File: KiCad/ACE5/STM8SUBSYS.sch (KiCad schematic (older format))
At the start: 4 parts, among them J400 48409-0003, J402 Conn_02x06_Odd_Even

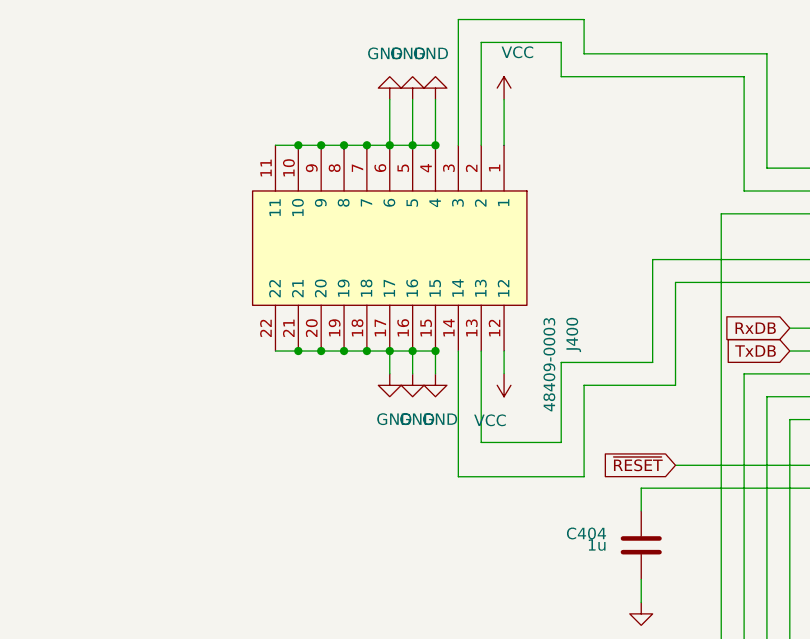
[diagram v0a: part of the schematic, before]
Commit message: Update ACE3NOKB to reflect errors in Mem Decode. ACE5NOKB test SMT ideas. Added 180 & 380.
Signed-off-by: John Bradley <flypie@rocketmail.com>
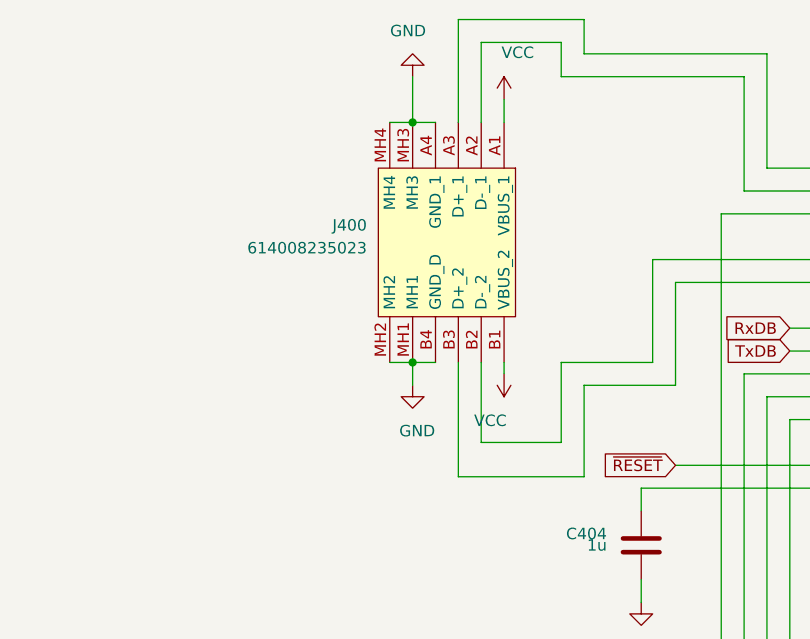
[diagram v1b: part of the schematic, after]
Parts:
- removed J400: 48409-0003, SamacSys_Parts:48409-0003, symbol SamacSys_Parts:48409-0003
- added J400: 614008235023, SamacSys_Parts:614008235023, symbol SamacSys_Parts:614008235023
- C404: footprint Capacitor_THT:C_Disc_D3.0mm_W1.6mm_P2.50mm -> Capacitor_SMD:C_1206_3216Metric
- J402: footprint Connector_PinHeader_2.54mm:PinHeader_2x06_P2.54mm_Vertical -> Connector_PinHeader_2.54mm:PinHeader_2x06_P2.54mm_Vertical_SMD
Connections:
- net GND: now also J400.A4 (GND_1), J400.B4 (GND_D), J400.MH1, J400.MH2, J400.MH3, J400.MH4
- net VCC: now also J400.A1 (VBUS_1), J400.B1 (VBUS_2)
- net at Z408.12 (PB4): now also J400.B2 (D-_2)
- net at Z408.11 (PB5): now also J400.B3 (D+_2)
- net at Z408.6 (PA2): now also J400.A2 (D-_1)
- net at Z408.5 (PA1): now also J400.A3 (D+_1)
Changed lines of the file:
@@
 	1    0    0    -1
 $EndComp
-Wire Wire Line
-	4100 3000 4100 2800
-$Comp
-L power:GND #~PWR0144
-U 1 1 6025F5D6
-P 4100 2800
-F 0 "#~PWR0144" H 4100 2550 50  0001 C CNN
-F 1 "GND" H 4120 2600 50  0000 C CNN
-F 2 "" H 4100 2800 50  0001 C CNN
-F 3 "" H 4100 2800 50  0001 C CNN
-	1    4100 2800
-	-1   0    0    1
-$EndComp
-Wire Wire Line
-	4200 3900 4200 4000
 $Comp
 L power:VCC #~PWR0145
@@
 	-1   0    0    1
 $EndComp
-Wire Wire Line
-	4600 3900 4600 4000
 $Comp
 L power:VCC #~PWR0146
@@
 	1    0    0    -1
 $EndComp
-Wire Wire Line
-	4600 3000 4600 2800
-Wire Wire Line
-	4200 3000 4200 2800
 $Comp
 L power:GND #~PWR0148
 U 1 1 602818B7
-P 4200 2800
-F 0 "#~PWR0148" H 4200 2550 50  0001 C CNN
-F 1 "GND" H 4220 2600 50  0000 C CNN
-F 2 "" H 4200 2800 50  0001 C CNN
-F 3 "" H 4200 2800 50  0001 C CNN
-	1    4200 2800
+P 4200 2700
+F 0 "#~PWR0148" H 4200 2450 50  0001 C CNN
+F 1 "GND" H 4220 2500 50  0000 C CNN
+F 2 "" H 4200 2700 50  0001 C CNN
+F 3 "" H 4200 2700 50  0001 C CNN
+	1    4200 2700
 	-1   0    0    1
 $EndComp
-$Comp
-L power:GND #~PWR0149
-U 1 1 602874B7
-P 4200 4000
-F 0 "#~PWR0149" H 4200 3750 50  0001 C CNN
-F 1 "GND" H 4220 3800 50  0000 C CNN
-F 2 "" H 4200 4000 50  0001 C CNN
-F 3 "" H 4200 4000 50  0001 C CNN
-	1    4200 4000
-	1    0    0    -1
-$EndComp
-Wire Wire Line
-	4100 3900 4100 4000
-$Comp
-L power:GND #~PWR0152
-U 1 1 602877B2
-P 4100 4000
-F 0 "#~PWR0152" H 4100 3750 50  0001 C CNN
-F 1 "GND" H 4120 3800 50  0000 C CNN
-F 2 "" H 4100 4000 50  0001 C CNN
-F 3 "" H 4100 4000 50  0001 C CNN
-	1    4100 4000
-	1    0    0    -1
-$EndComp
 Wire Wire Line
 	5950 3100 5750 3100
@@
 Wire Wire Line
 	5350 3600 5950 3600
-$Comp
-L SamacSys_Parts:48409-0003 J400
-U 1 1 60165D46
-P 4600 3000
-F 0 "J400" H 5350 3300 50  0000 L CNN
-F 1 "48409-0003" H 5350 3200 50  0000 L CNN
-F 2 "SamacSys_Parts:48409-0003" H 5350 3100 50  0001 L CNN
-F 3 "http://www.molex.com/pdm_docs/sd/484090003_sd.pdf" H 5350 3000 50  0001 L CNN
-F 4 "2 port Vertical Through Hole Version 3 Type A USB Connector" H 5350 2900 50  0001 L CNN "Description"
-F 5 "" H 5350 2800 50  0001 L CNN "Height"
-F 6 "538-48409-0003" H 5350 2700 50  0001 L CNN "Mouser Part Number"
-F 7 "https://www.mouser.co.uk/ProductDetail/Molex/48409-0003/?qs=KpdAywxU012gZlXxUSovmw%3D%3D" H 5350 2600 50  0001 L CNN "Mouser Price/Stock"
-F 8 "Molex" H 5350 2500 50  0001 L CNN "Manufacturer_Name"
-F 9 "48409-0003" H 5350 2400 50  0001 L CNN "Manufacturer_Part_Number"
-	1    4600 3000
-	0    1    1    0
-$EndComp
 Wire Wire Line
 	4850 2550 4850 2700
@@
 	4950 2450 4400 2450
 Wire Wire Line
-	4400 2450 4400 3000
-Wire Wire Line
 	4950 2600 5750 2600
 Wire Wire Line
-	4500 2550 4500 3000
-Wire Wire Line
 	4850 3950 4850 4300
 Wire Wire Line
-	4850 4300 4500 4300
-Wire Wire Line
-	4500 4300 4500 3900
-Wire Wire Line
 	4850 3950 5250 3950
 Wire Wire Line
 	4950 4050 4950 4450
 Wire Wire Line
-	4950 4450 4400 4450
-Wire Wire Line
-	4400 4450 4400 3900
-Wire Wire Line
 	4950 4050 5350 4050
 Wire Wire Line
 	4500 2550 4850 2550
-Wire Wire Line
-	4300 3000 4300 2800
-$Comp
-L power:GND #~PWR0163
-U 1 1 6021458D
-P 4300 2800
-F 0 "#~PWR0163" H 4300 2550 50  0001 C CNN
-F 1 "GND" H 4320 2600 50  0000 C CNN
-F 2 "" H 4300 2800 50  0001 C CNN
-F 3 "" H 4300 2800 50  0001 C CNN
-	1    4300 2800
-	-1   0    0    1
-$EndComp
-Wire Wire Line
-	4300 3900 4300 4000
-$Comp
-L power:GND #~PWR0165
-U 1 1 602439CD
-P 4300 4000
-F 0 "#~PWR0165" H 4300 3750 50  0001 C CNN
-F 1 "GND" H 4320 3800 50  0000 C CNN
-F 2 "" H 4300 4000 50  0001 C CNN
-F 3 "" H 4300 4000 50  0001 C CNN
-	1    4300 4000
-	1    0    0    -1
-$EndComp
 Text GLabel 5850 3800 0    50   Input ~ 0
 RxDB
@@
 	5950 3900 5850 3900
 Wire Wire Line
-	4300 3000 4200 3000
-Connection ~ 4300 3000
-Connection ~ 3700 3000
-Wire Wire Line
-	3700 3000 3600 3000
-Connection ~ 3800 3000
-Wire Wire Line
-	3800 3000 3700 3000
-Connection ~ 3900 3000
-Wire Wire Line
-	3900 3000 3800 3000
-Connection ~ 4000 3000
-Wire Wire Line
-	4000 3000 3900 3000
-Connection ~ 4100 3000
-Wire Wire Line
-	4100 3000 4000 3000
-Connection ~ 4200 3000
-Wire Wire Line
-	4200 3000 4100 3000
-Wire Wire Line
-	4300 3900 4200 3900
-Connection ~ 4300 3900
-Connection ~ 3700 3900
-Wire Wire Line
-	3700 3900 3600 3900
-Connection ~ 3800 3900
-Wire Wire Line
-	3800 3900 3700 3900
-Connection ~ 3900 3900
-Wire Wire Line
-	3900 3900 3800 3900
-Connection ~ 4000 3900
-Wire Wire Line
-	4000 3900 3900 3900
-Connection ~ 4100 3900
-Wire Wire Line
-	4100 3900 4000 3900
-Connection ~ 4200 3900
-Wire Wire Line
-	4200 3900 4100 3900
-Wire Wire Line
 	6200 5900 6300 5900
 Wire Wire Line
 	6800 5900 6900 5900
 $Comp
-L power:GND #~PWR?
+L power:GND #~PWR0164
 U 1 1 602D5919
 P 6900 5900
-AR Path="/5D919407/602D5919" Ref="#~PWR?"  Part="1"
-AR Path="/601B15FC/602D5919" Ref="#~PWR0164"  Part="1"
-AR Path="/604875AE/602D5919" Ref="#~PWR0164"  Part="1"
 F 0 "#~PWR0164" H 6900 5650 50  0001 C CNN
 F 1 "GND" V 6950 5750 50  0000 R CNN
@@
 $EndComp
 $Comp
-L power:VCC #~PWR?
+L power:VCC #~PWR0166
 U 1 1 602D591F
 P 6200 5900
-AR Path="/5D919407/602D591F" Ref="#~PWR?"  Part="1"
-AR Path="/601B15FC/602D591F" Ref="#~PWR0166"  Part="1"
-AR Path="/604875AE/602D591F" Ref="#~PWR0166"  Part="1"
 F 0 "#~PWR0166" H 6200 5750 50  0001 C CNN
 F 1 "VCC" V 6250 6050 50  0000 L CNN
@@
 $EndComp
 $Comp
-L Connector_Generic:Conn_02x06_Odd_Even J?
+L Connector_Generic:Conn_02x06_Odd_Even J402
 U 1 1 602D5927
 P 6500 5600
-AR Path="/5D919407/602D5927" Ref="J?"  Part="1"
-AR Path="/601B15FC/602D5927" Ref="J402"  Part="1"
-AR Path="/604875AE/602D5927" Ref="J402"  Part="1"
 F 0 "J402" H 6550 5150 50  0000 C CNN
 F 1 "Conn_02x06_Odd_Even" H 6550 5050 50  0000 C CNN
-F 2 "Connector_PinHeader_2.54mm:PinHeader_2x06_P2.54mm_Vertical" H 6500 5600 50  0001 C CNN
+F 2 "Connector_PinHeader_2.54mm:PinHeader_2x06_P2.54mm_Vertical_SMD" H 6500 5600 50  0001 C CNN
 F 3 "" H 6500 5600 50  0001 C CNN
 F 4 "SAMTEC" H 6500 5600 50  0001 C CNN "Manufacturer_Name"
@@
 F 0 "C404" H 5050 4800 50  0000 R CNN
 F 1 "1u" H 5050 4750 50  0000 R CNN
-F 2 "Capacitor_THT:C_Disc_D3.0mm_W1.6mm_P2.50mm" H 5200 4750 50  0001 C CNN
+F 2 "Capacitor_SMD:C_1206_3216Metric" H 5200 4750 50  0001 C CNN
 F 3 "~" H 5200 4750 50  0001 C CNN
 	1    5200 4750
@@
 Wire Wire Line
 	5550 5700 6300 5700
+Connection ~ 4200 3950
+Wire Wire Line
+	4300 3950 4200 3950
+$Comp
+L power:GND #~PWR0149
+U 1 1 602874B7
+P 4200 4050
+F 0 "#~PWR0149" H 4200 3800 50  0001 C CNN
+F 1 "GND" H 4220 3850 50  0000 C CNN
+F 2 "" H 4200 4050 50  0001 C CNN
+F 3 "" H 4200 4050 50  0001 C CNN
+	1    4200 4050
+	1    0    0    -1
+$EndComp
+Wire Wire Line
+	4200 3950 4200 4050
+Wire Wire Line
+	4100 3950 4200 3950
+Wire Wire Line
+	4600 3950 4600 4000
+Wire Wire Line
+	4950 4450 4400 4450
+Wire Wire Line
+	4850 4300 4500 4300
+Wire Wire Line
+	4200 2900 4100 2900
+Connection ~ 4200 2900
+Wire Wire Line
+	4200 2900 4200 2700
+Wire Wire Line
+	4400 4450 4400 3950
+Wire Wire Line
+	4500 4300 4500 3950
+Wire Wire Line
+	4300 2900 4200 2900
+Wire Wire Line
+	4400 2450 4400 2900
+Wire Wire Line
+	4500 2550 4500 2900
+Wire Wire Line
+	4600 2900 4600 2800
+$Comp
+L SamacSys_Parts:614008235023 J400
+U 1 1 6023FC0E
+P 4650 3100
+F 0 "J400" V 4900 2450 50  0000 R CNN
+F 1 "614008235023" V 5000 2450 50  0000 R CNN
+F 2 "SamacSys_Parts:614008235023" H 6900 2750 50  0001 L CNN
+F 3 "http://katalog.we-online.de/em/datasheet/614008235023.pdf" H 6900 2650 50  0001 L CNN
+F 4 "Wurth Elektronik WR-COM Series, Type A USB Connector, Receptacle" H 6900 2550 50  0001 L CNN "Description"
+F 5 "16" H 7050 2450 50  0001 L CNN "Height"
+F 6 "710-614008235023" H 6900 2350 50  0001 L CNN "Mouser Part Number"
+F 7 "https://www.mouser.co.uk/ProductDetail/Wurth-Elektronik/614008235023/?qs=rS3zZhy2AQP6TSxAYKTnAw%3D%3D" H 6900 2250 50  0001 L CNN "Mouser Price/Stock"
+F 8 "Wurth Elektronik" H 6900 2150 50  0001 L CNN "Manufacturer_Name"
+F 9 "614008235023" H 6900 2050 50  0001 L CNN "Manufacturer_Part_Number"
+	1    4650 3100
+	0    1    1    0
+$EndComp
 $EndSCHEMATC

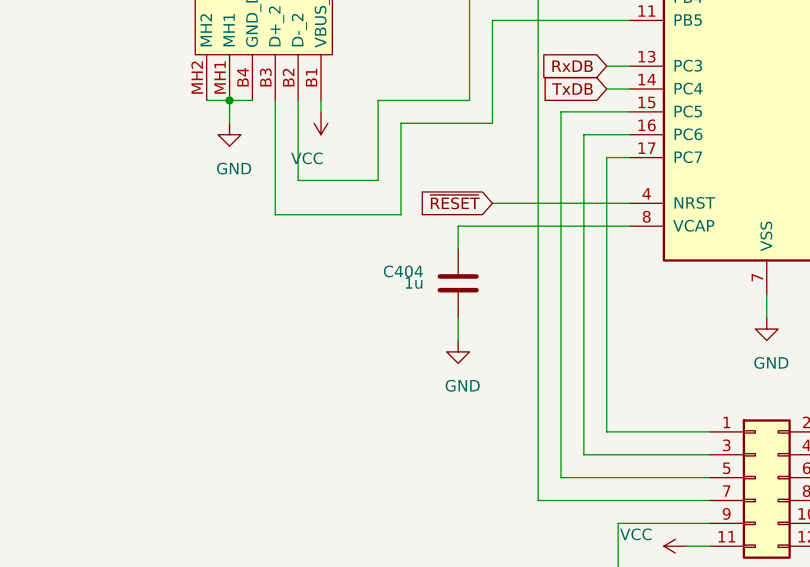
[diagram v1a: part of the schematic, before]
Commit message: Fix several problems with Chip Select. Reconnect the Data bus for the VDG to the CPU bus which has become disconnected.
Signed-off-by: John Bradley <flypie@rocketmail.com>
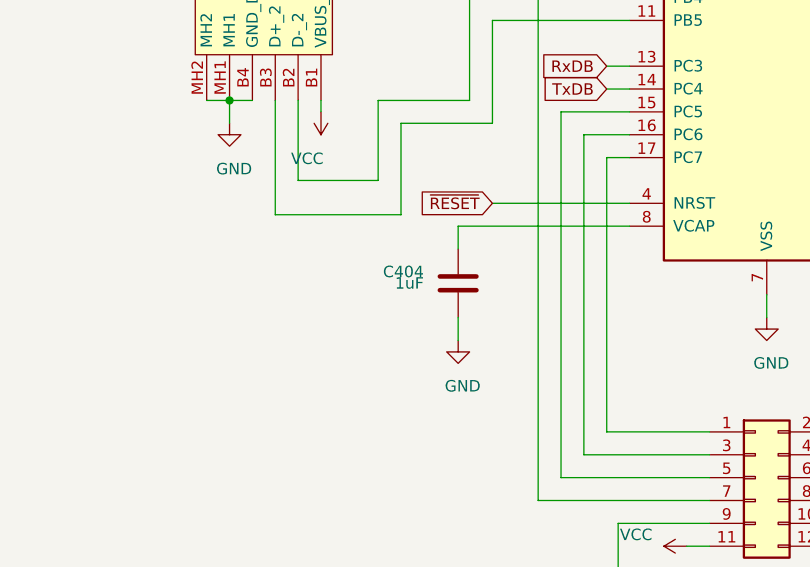
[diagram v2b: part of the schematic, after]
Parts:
- C404: value 1u -> 1uF; Manufacturer_Name (none) -> Vishay / Vitramon; Manufacturer_Part_Number (none) -> VJ1206Y105KXATW1BC
- J402: Manufacturer_Name SAMTEC -> Molex; Manufacturer_Part_Number HTSW-106-08-S-D -> 15-91-0120
- Z408: Manufacturer_Name (none) -> STMicroelectronics; Manufacturer_Part_Number (none) -> STM8S003F3P6TR
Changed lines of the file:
@@
 F 2 "Package_SO:TSSOP-20_4.4x6.5mm_P0.65mm" H 6600 4900 50  0001 L CNN
 F 3 "http://www.st.com/st-web-ui/static/active/en/resource/technical/document/datasheet/DM00024550.pdf" H 6500 3400 50  0001 C CNN
+F 4 "STMicroelectronics" H 6550 3800 50  0001 C CNN "Manufacturer_Name"
+F 5 "STM8S003F3P6TR" H 6550 3800 50  0001 C CNN "Manufacturer_Part_Number"
 	1    6550 3800
 	1    0    0    -1
@@
 F 2 "Connector_PinHeader_2.54mm:PinHeader_2x06_P2.54mm_Vertical_SMD" H 6500 5600 50  0001 C CNN
 F 3 "" H 6500 5600 50  0001 C CNN
-F 4 "SAMTEC" H 6500 5600 50  0001 C CNN "Manufacturer_Name"
-F 5 "HTSW-106-08-S-D " H 6500 5600 50  0001 C CNN "Manufacturer_Part_Number"
+F 4 "Molex" H 6500 5600 50  0001 C CNN "Manufacturer_Name"
+F 5 "15-91-0120 " H 6500 5600 50  0001 C CNN "Manufacturer_Part_Number"
 	1    6500 5600
 	1    0    0    -1
@@
 P 5200 4750
 F 0 "C404" H 5050 4800 50  0000 R CNN
-F 1 "1u" H 5050 4750 50  0000 R CNN
+F 1 "1uF" H 5050 4750 50  0000 R CNN
 F 2 "Capacitor_SMD:C_1206_3216Metric" H 5200 4750 50  0001 C CNN
 F 3 "~" H 5200 4750 50  0001 C CNN
+F 4 "Vishay / Vitramon" H 5200 4750 50  0001 C CNN "Manufacturer_Name"
+F 5 "VJ1206Y105KXATW1BC" H 5200 4750 50  0001 C CNN "Manufacturer_Part_Number"
 	1    5200 4750
 	1    0    0    -1
